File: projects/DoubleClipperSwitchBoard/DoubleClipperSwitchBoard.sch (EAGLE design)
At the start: 12 parts

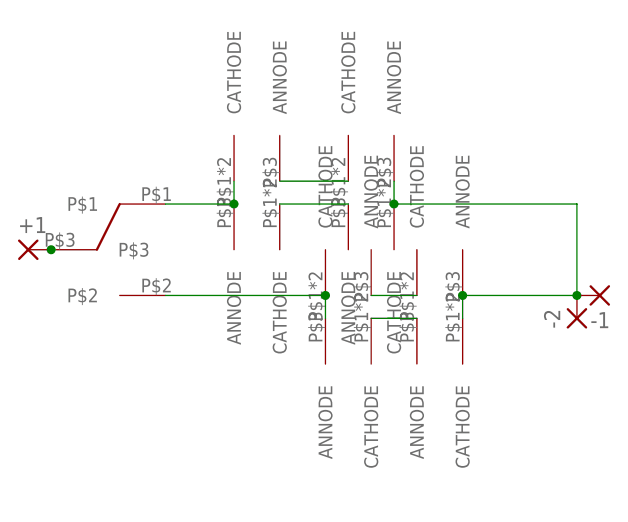
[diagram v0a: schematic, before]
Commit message: Updated to use new clipper block.
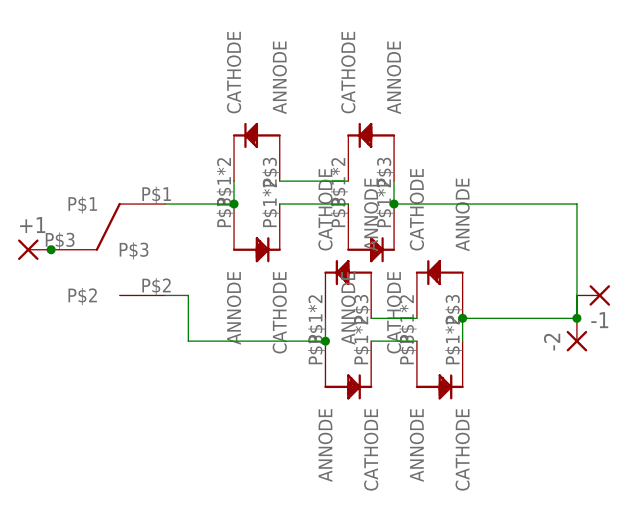
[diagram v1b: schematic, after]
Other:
- moved on the sheet: -2
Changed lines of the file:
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@@
 <instance part="D2" gate="G$1" x="45.72" y="63.5"/>
 <instance part="D1" gate="G$1" x="40.64" y="60.96" rot="R180"/>
-<instance part="U$4" gate="G$1" x="55.88" y="50.8"/>
-<instance part="U$5" gate="G$1" x="50.8" y="48.26" rot="R180"/>
+<instance part="U$4" gate="G$1" x="55.88" y="48.26"/>
+<instance part="U$5" gate="G$1" x="50.8" y="45.72" rot="R180"/>
 <instance part="+1" gate="1" x="17.78" y="55.88"/>
-<instance part="-2" gate="1" x="78.74" y="48.26" rot="R90"/>
+<instance part="-2" gate="1" x="78.74" y="45.72" rot="R90"/>
 <instance part="-1" gate="1" x="81.28" y="50.8" rot="R180"/>
 <instance part="D4" gate="G$1" x="58.42" y="63.5"/>
 <instance part="D3" gate="G$1" x="53.34" y="60.96" rot="R180"/>
-<instance part="U$8" gate="G$1" x="66.04" y="50.8"/>
-<instance part="U$9" gate="G$1" x="60.96" y="48.26" rot="R180"/>
+<instance part="U$8" gate="G$1" x="66.04" y="48.26"/>
+<instance part="U$9" gate="G$1" x="60.96" y="45.72" rot="R180"/>
 </instances>
 <busses>
@@
 <pinref part="U$4" gate="G$1" pin="CATHODE"/>
 <pinref part="U$5" gate="G$1" pin="ANNODE"/>
-<wire x1="50.8" y1="48.26" x2="50.8" y2="50.8" width="0.1524" layer="91"/>
+<wire x1="50.8" y1="45.72" x2="50.8" y2="48.26" width="0.1524" layer="91"/>
 <pinref part="U$1" gate="G$1" pin="P$2"/>
-<wire x1="33.02" y1="50.8" x2="50.8" y2="50.8" width="0.1524" layer="91"/>
-<junction x="50.8" y="50.8"/>
+<wire x1="33.02" y1="50.8" x2="35.56" y2="50.8" width="0.1524" layer="91"/>
+<wire x1="35.56" y1="50.8" x2="35.56" y2="45.72" width="0.1524" layer="91"/>
+<wire x1="35.56" y1="45.72" x2="50.8" y2="45.72" width="0.1524" layer="91"/>
+<junction x="50.8" y="45.72"/>
 </segment>
 </net>
@@
 <pinref part="U$4" gate="G$1" pin="ANNODE"/>
 <pinref part="U$8" gate="G$1" pin="CATHODE"/>
-<wire x1="55.88" y1="50.8" x2="60.96" y2="50.8" width="0.1524" layer="91"/>
+<wire x1="55.88" y1="48.26" x2="60.96" y2="48.26" width="0.1524" layer="91"/>
 </segment>
 </net>
@@
 <pinref part="U$8" gate="G$1" pin="ANNODE"/>
 <pinref part="U$9" gate="G$1" pin="CATHODE"/>
-<wire x1="66.04" y1="48.26" x2="66.04" y2="50.8" width="0.1524" layer="91"/>
+<wire x1="66.04" y1="45.72" x2="66.04" y2="48.26" width="0.1524" layer="91"/>
 <pinref part="-2" gate="1" pin="P"/>
 <pinref part="-1" gate="1" pin="P"/>
-<wire x1="66.04" y1="50.8" x2="78.74" y2="50.8" width="0.1524" layer="91"/>
-<junction x="66.04" y="50.8"/>
-<junction x="78.74" y="50.8"/>
+<wire x1="66.04" y1="48.26" x2="78.74" y2="48.26" width="0.1524" layer="91"/>
+<junction x="66.04" y="48.26"/>
+<junction x="78.74" y="48.26"/>
 <wire x1="58.42" y1="60.96" x2="78.74" y2="60.96" width="0.1524" layer="91"/>
-<wire x1="78.74" y1="60.96" x2="78.74" y2="50.8" width="0.1524" layer="91"/>
+<wire x1="78.74" y1="60.96" x2="78.74" y2="48.26" width="0.1524" layer="91"/>
 <junction x="58.42" y="60.96"/>
+<wire x1="78.74" y1="48.26" x2="78.74" y2="50.8" width="0.1524" layer="91"/>
 </segment>
 </net>
@@
 <pinref part="U$5" gate="G$1" pin="CATHODE"/>
 <pinref part="U$9" gate="G$1" pin="ANNODE"/>
-<wire x1="55.88" y1="48.26" x2="60.96" y2="48.26" width="0.1524" layer="91"/>
+<wire x1="55.88" y1="45.72" x2="60.96" y2="45.72" width="0.1524" layer="91"/>
 </segment>
 </net>
